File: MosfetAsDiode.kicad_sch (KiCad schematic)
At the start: 4 parts, among them Q1 IRF3205, Q2 IRF3205

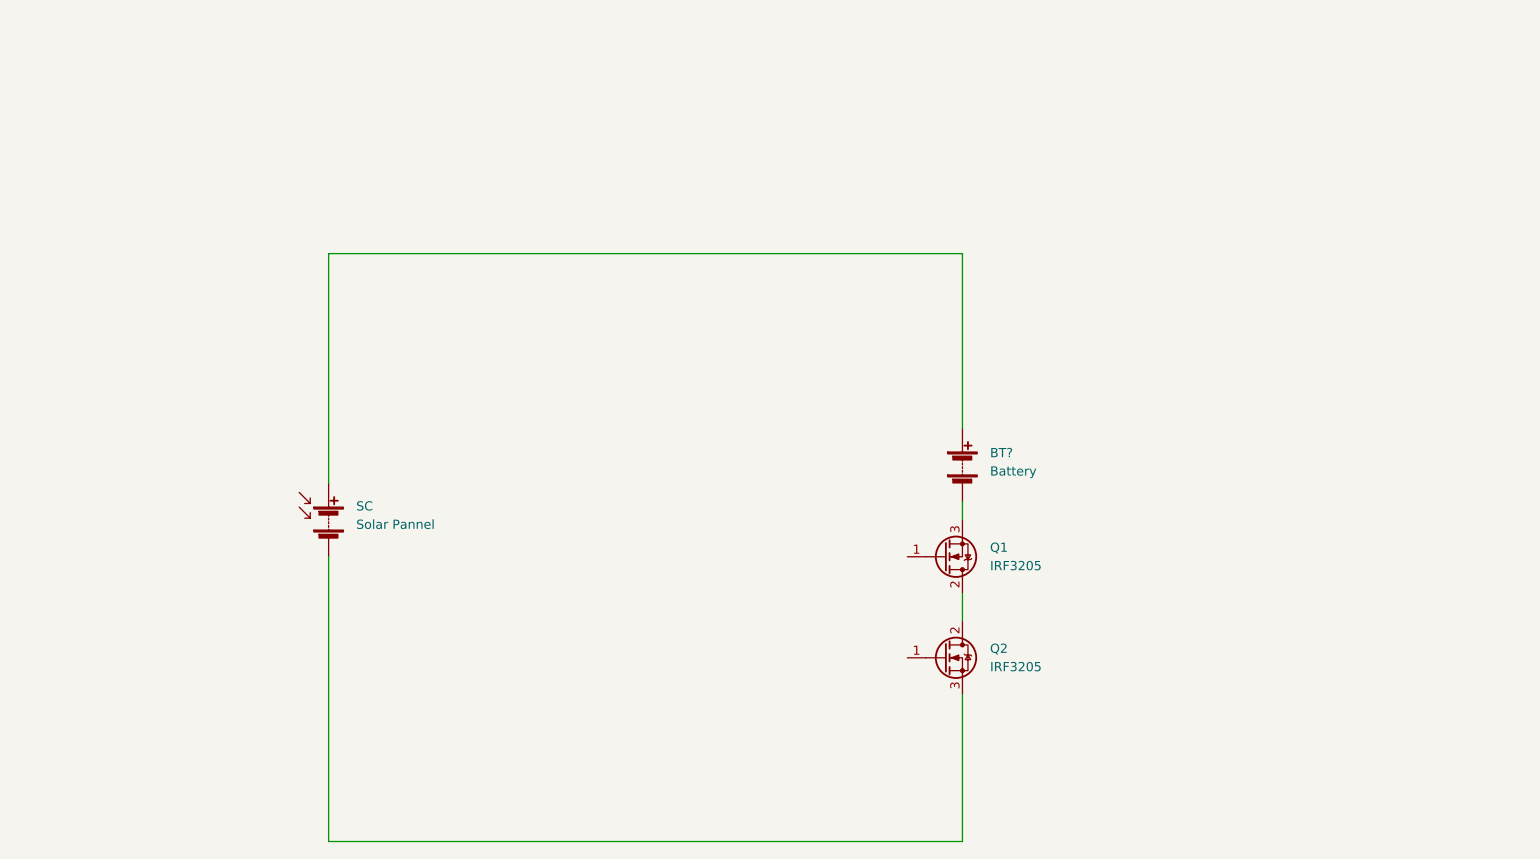
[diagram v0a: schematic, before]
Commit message: Updates after testing the gate with a positive voltage
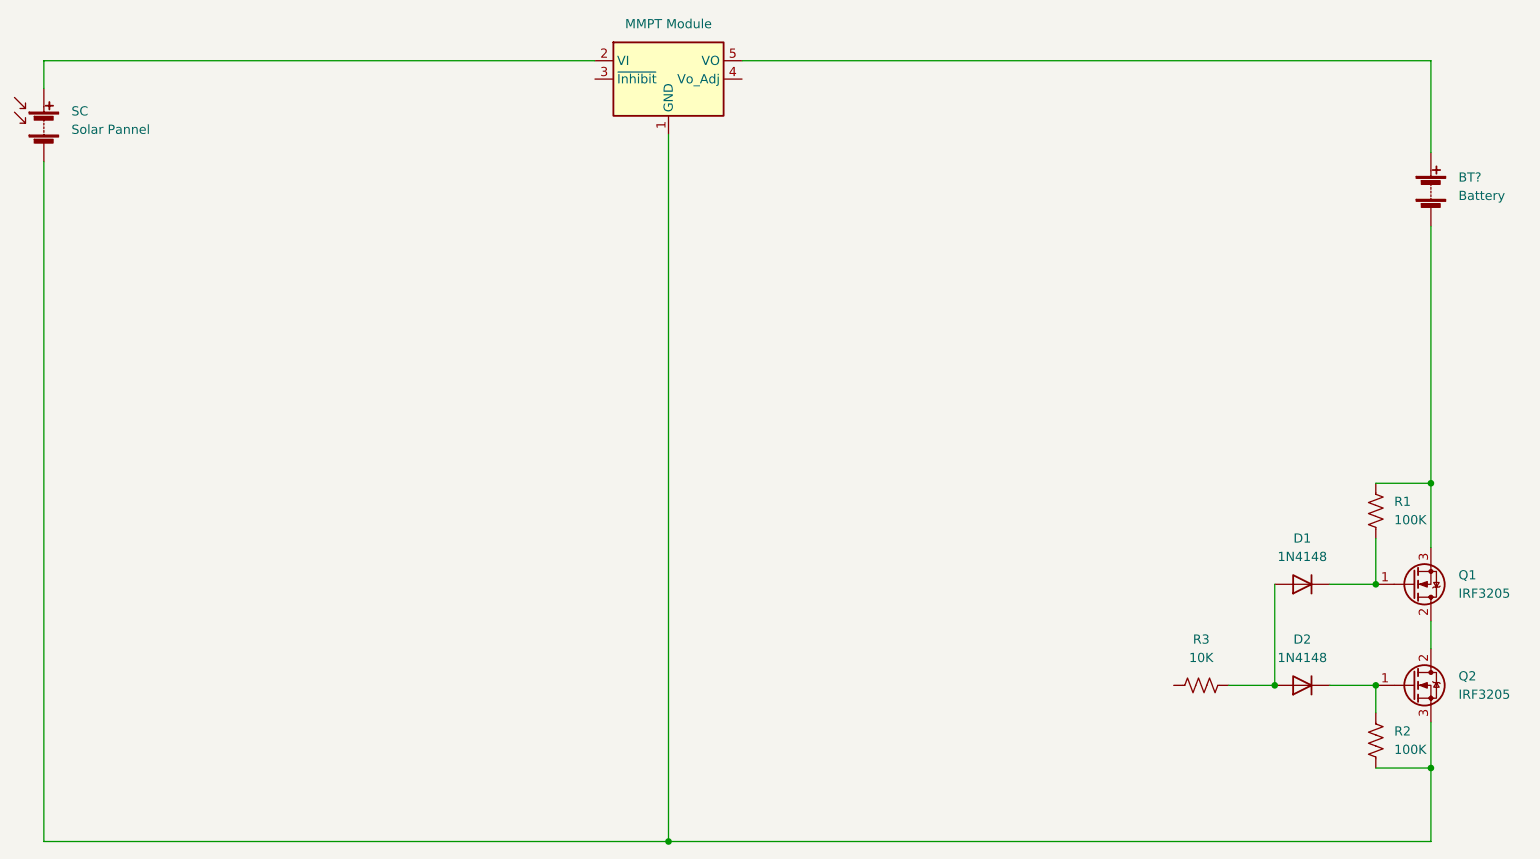
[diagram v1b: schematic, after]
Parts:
- added D1, D2: 1N4148, Diode_THT:D_DO-35_SOD27_P7.62mm_Horizontal, symbol Diode:1N4148
- added R1, R2: 100K, symbol Device:R_US
- added R3: 10K, symbol Device:R_US
- added U?: MMPT Module, Module:Texas_EUS_R-PDSS-T5_THT, symbol Converter_DCDC:PTN78000H_EUS-5
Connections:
- net at Q1.1 (G): now also D1.1 (K), R1.2
- net at BT?.2 (-), Q1.3 (S): now also R1.1
- net at SC.1 (+): now also U?.2 (VI); no longer BT?.1 (+)
- net at Q2.3 (S), SC.2 (-): now also R2.2, U?.1 (GND)
- net at Q2.1 (G): now also D2.1 (K), R2.1
- new net: D1.2 (A), D2.2 (A), R3.2
- new net: BT?.1 (+), U?.5 (VO)
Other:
- moved on the sheet: BT?, Q1, Q2, SC

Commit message: adding zener and led
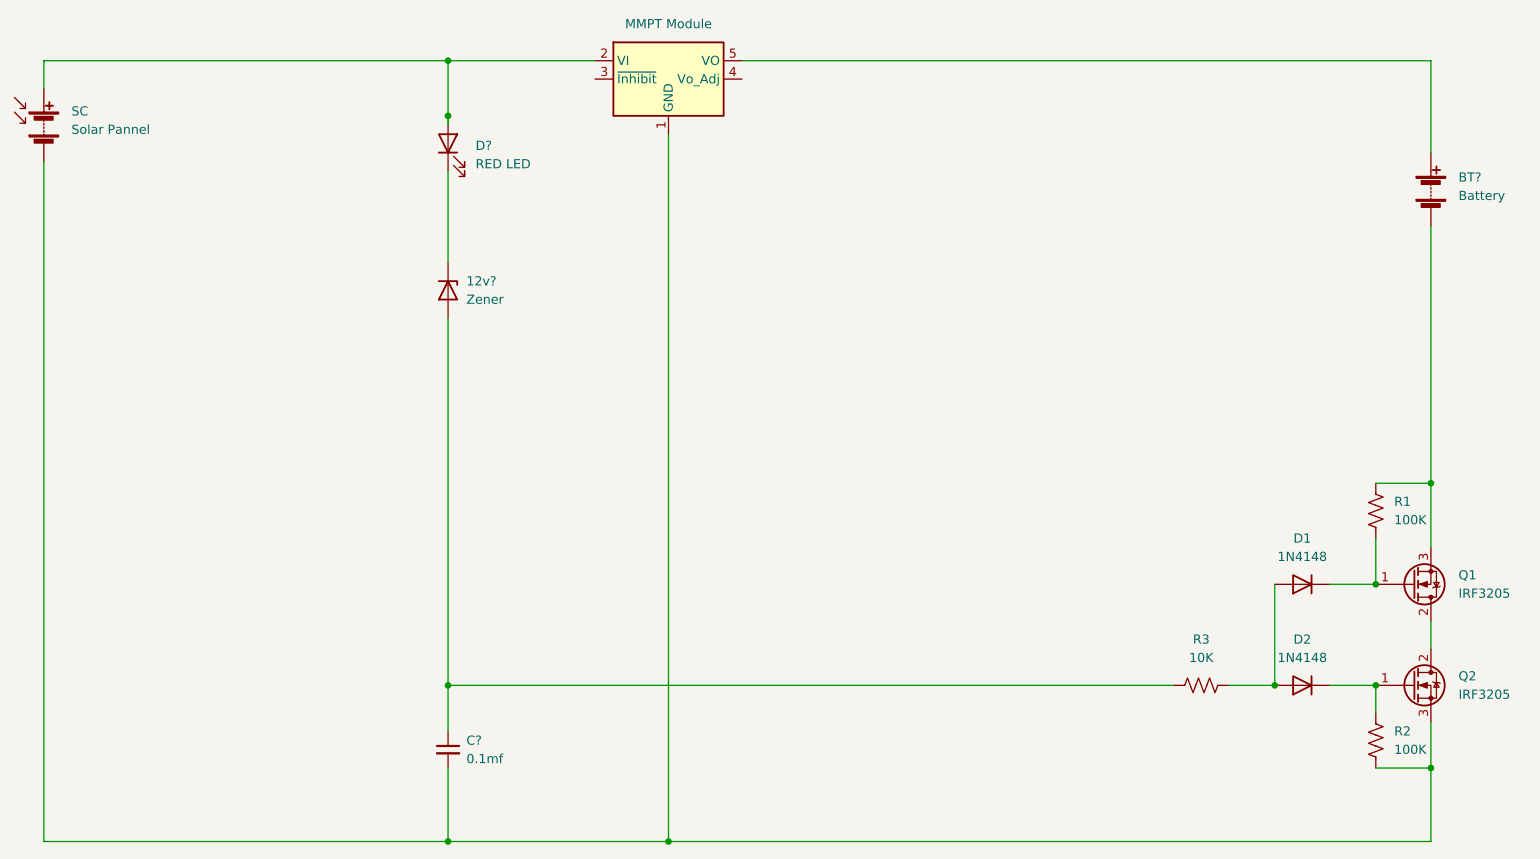
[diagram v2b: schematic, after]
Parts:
- added 12v?: Zener, symbol Device:D_Zener
- added C?: 0.1mf, symbol Device:C_Small
- added D?: RED LED, symbol Device:LED
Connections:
- net at SC.1 (+), U?.2 (VI): now also D?.2 (A)
- net at Q2.3 (S), R2.2, SC.2 (-)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: now also C?.2
- net at R3.1: now also 12v?.2 (A), C?.1
- new net: 12v?.1 (K), D?.1 (K)
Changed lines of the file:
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@@
     (comment 2 "https://d3i71xaburhd42.cloudfront.net/47d21f9b2ac4e8fc369e9b3f34bbec2c18305c72/250px/1-Figure1-1.png")
   )
+  (junction (at 80.01 139.7) (diameter 0) (color 0 0 0 0)
+  )
   (junction (at 194.31 118.11) (diameter 0) (color 0 0 0 0)
   )
@@
   (junction (at 215.9 90.17) (diameter 0) (color 0 0 0 0)
   )
+  (junction (at 80.01 39.37) (diameter 0) (color 0 0 0 0)
+  )
   (junction (at 208.28 104.14) (diameter 0) (color 0 0 0 0)
   )
+  (junction (at 80.01 118.11) (diameter 0) (color 0 0 0 0)
+  )
   (junction (at 215.9 129.54) (diameter 0) (color 0 0 0 0)
   )
+  (junction (at 80.01 31.75) (diameter 0) (color 0 0 0 0)
+  )
   (junction (at 110.49 139.7) (diameter 0) (color 0 0 0 0)
   )
@@
     (stroke (width 0) (type default) (color 0 0 0 0))
   )
+  (wire (pts (xy 180.34 118.11) (xy 80.01 118.11))
+    (stroke (width 0) (type default) (color 0 0 0 0))
+  )
+  (wire (pts (xy 80.01 129.54) (xy 80.01 139.7))
+    (stroke (width 0) (type default) (color 0 0 0 0))
+  )
+  (wire (pts (xy 80.01 31.75) (xy 100.33 31.75))
+    (stroke (width 0) (type default) (color 0 0 0 0))
+  )
   (wire (pts (xy 215.9 90.17) (xy 215.9 99.06))
     (stroke (width 0) (type default) (color 0 0 0 0))
   )
+  (wire (pts (xy 80.01 118.11) (xy 80.01 124.46))
+    (stroke (width 0) (type default) (color 0 0 0 0))
+  )
   (wire (pts (xy 215.9 54.61) (xy 215.9 90.17))
     (stroke (width 0) (type default) (color 0 0 0 0))
@@
     (stroke (width 0) (type default) (color 0 0 0 0))
   )
+  (wire (pts (xy 80.01 31.75) (xy 80.01 39.37))
+    (stroke (width 0) (type default) (color 0 0 0 0))
+  )
   (wire (pts (xy 215.9 129.54) (xy 215.9 123.19))
     (stroke (width 0) (type default) (color 0 0 0 0))
   )
-  (wire (pts (xy 24.13 31.75) (xy 100.33 31.75))
+  (wire (pts (xy 24.13 31.75) (xy 80.01 31.75))
+    (stroke (width 0) (type default) (color 0 0 0 0))
+  )
+  (wire (pts (xy 80.01 46.99) (xy 80.01 59.69))
     (stroke (width 0) (type default) (color 0 0 0 0))
   )
@@
     (stroke (width 0) (type default) (color 0 0 0 0))
   )
+  (wire (pts (xy 24.13 139.7) (xy 80.01 139.7))
+    (stroke (width 0) (type default) (color 0 0 0 0))
+  )
   (wire (pts (xy 208.28 90.17) (xy 215.9 90.17))
     (stroke (width 0) (type default) (color 0 0 0 0))
   )
-  (wire (pts (xy 24.13 139.7) (xy 110.49 139.7))
-    (stroke (width 0) (type default) (color 0 0 0 0))
-  )
   (wire (pts (xy 120.65 31.75) (xy 215.9 31.75))
     (stroke (width 0) (type default) (color 0 0 0 0))
@@
   )
   (wire (pts (xy 194.31 104.14) (xy 194.31 118.11))
+    (stroke (width 0) (type default) (color 0 0 0 0))
+  )
+  (wire (pts (xy 80.01 67.31) (xy 80.01 118.11))
+    (stroke (width 0) (type default) (color 0 0 0 0))
+  )
+  (wire (pts (xy 80.01 139.7) (xy 110.49 139.7))
+    (stroke (width 0) (type default) (color 0 0 0 0))
+  )
+  (wire (pts (xy 80.01 39.37) (xy 80.01 40.64))
     (stroke (width 0) (type default) (color 0 0 0 0))
   )
@@
     (pin "2")
     (pin "3")
+  )
+  (symbol (lib_id "Device:LED") (at 80.01 43.18 90) (unit 1)
+    (in_bom yes) (on_board yes) (fields_autoplaced)
+    (property "Reference" "D?" (id 0) (at 83.82 43.4974 90)
+      (effects (font (size 1.27 1.27)) (justify right))
+    )
+    (property "Value" "RED LED" (id 1) (at 83.82 46.0374 90)
+      (effects (font (size 1.27 1.27)) (justify right))
+    )
+    (property "Footprint" "" (id 2) (at 80.01 43.18 0)
+      (effects (font (size 1.27 1.27)) hide)
+    )
+    (property "Datasheet" "~" (id 3) (at 80.01 43.18 0)
+      (effects (font (size 1.27 1.27)) hide)
+    )
+    (pin "1")
+    (pin "2")
   )
   (symbol (lib_id "Diode:1N4148") (at 198.12 118.11 180) (unit 1)
@@
     (pin "2")
   )
+  (symbol (lib_id "Device:C_Small") (at 80.01 127 0) (unit 1)
+    (in_bom yes) (on_board yes) (fields_autoplaced)
+    (property "Reference" "C?" (id 0) (at 82.55 125.7362 0)
+      (effects (font (size 1.27 1.27)) (justify left))
+    )
+    (property "Value" "0.1mf" (id 1) (at 82.55 128.2762 0)
+      (effects (font (size 1.27 1.27)) (justify left))
+    )
+    (property "Footprint" "" (id 2) (at 80.01 127 0)
+      (effects (font (size 1.27 1.27)) hide)
+    )
+    (property "Datasheet" "~" (id 3) (at 80.01 127 0)
+      (effects (font (size 1.27 1.27)) hide)
+    )
+    (pin "1")
+    (pin "2")
+  )
   (symbol (lib_id "Transistor_FET:IRF3205") (at 213.36 118.11 0) (unit 1)
     (in_bom yes) (on_board yes) (fields_autoplaced)
@@
     (pin "2")
   )
+  (symbol (lib_id "Device:D_Zener") (at 80.01 63.5 270) (unit 1)
+    (in_bom yes) (on_board yes) (fields_autoplaced)
+    (property "Reference" "12v?" (id 0) (at 82.55 62.2299 90)
+      (effects (font (size 1.27 1.27)) (justify left))
+    )
+    (property "Value" "Zener" (id 1) (at 82.55 64.7699 90)
+      (effects (font (size 1.27 1.27)) (justify left))
+    )
+    (property "Footprint" "" (id 2) (at 80.01 63.5 0)
+      (effects (font (size 1.27 1.27)) hide)
+    )
+    (property "Datasheet" "~" (id 3) (at 80.01 63.5 0)
+      (effects (font (size 1.27 1.27)) hide)
+    )
+    (pin "1")
+    (pin "2")
+  )
   (symbol (lib_id "Device:R_US") (at 208.28 125.73 0) (unit 1)
     (in_bom yes) (on_board yes) (fields_autoplaced)
@@
   )
   (symbol_instances
+    (path "/8c56a9d4-3d74-41b6-867a-9e5b03646366"
+      (reference "12v?") (unit 1) (value "Zener") (footprint "")
+    )
     (path "/8637964f-65af-4a7c-8331-af34ceae9183"
       (reference "BT?") (unit 1) (value "Battery") (footprint "")
     )
+    (path "/6b04edba-d43e-4cc0-a03a-f6695b2e81d5"
+      (reference "C?") (unit 1) (value "0.1mf") (footprint "")
+    )
     (path "/7ff53ce7-3b96-4229-89d1-8f8a87153527"
       (reference "D1") (unit 1) (value "1N4148") (footprint "Diode_THT:D_DO-35_SOD27_P7.62mm_Horizontal")
@@
       (reference "D2") (unit 1) (value "1N4148") (footprint "Diode_THT:D_DO-35_SOD27_P7.62mm_Horizontal")
     )
+    (path "/28637788-f991-4e02-bbe8-3ca3781fa436"
+      (reference "D?") (unit 1) (value "RED LED") (footprint "")
+    )
     (path "/0f31f11f-c374-4640-b9a4-07bbdba8d354"
